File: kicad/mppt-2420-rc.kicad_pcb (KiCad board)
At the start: 4 copper layers, 67.7 x 86.4 mm, 121 parts, among them J1 MKDS 5/ 2-9,5, J2 MKDS 5/ 2-9,5, J3 8P8C, J4 8P8C, J5 Phoenix Contact MC 1,5, J7 UEXT, Q1 IPA045N10N3G, Q2 IPA045N10N3G, Q8 IRF135B203, Q9 DMP10H4D2S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

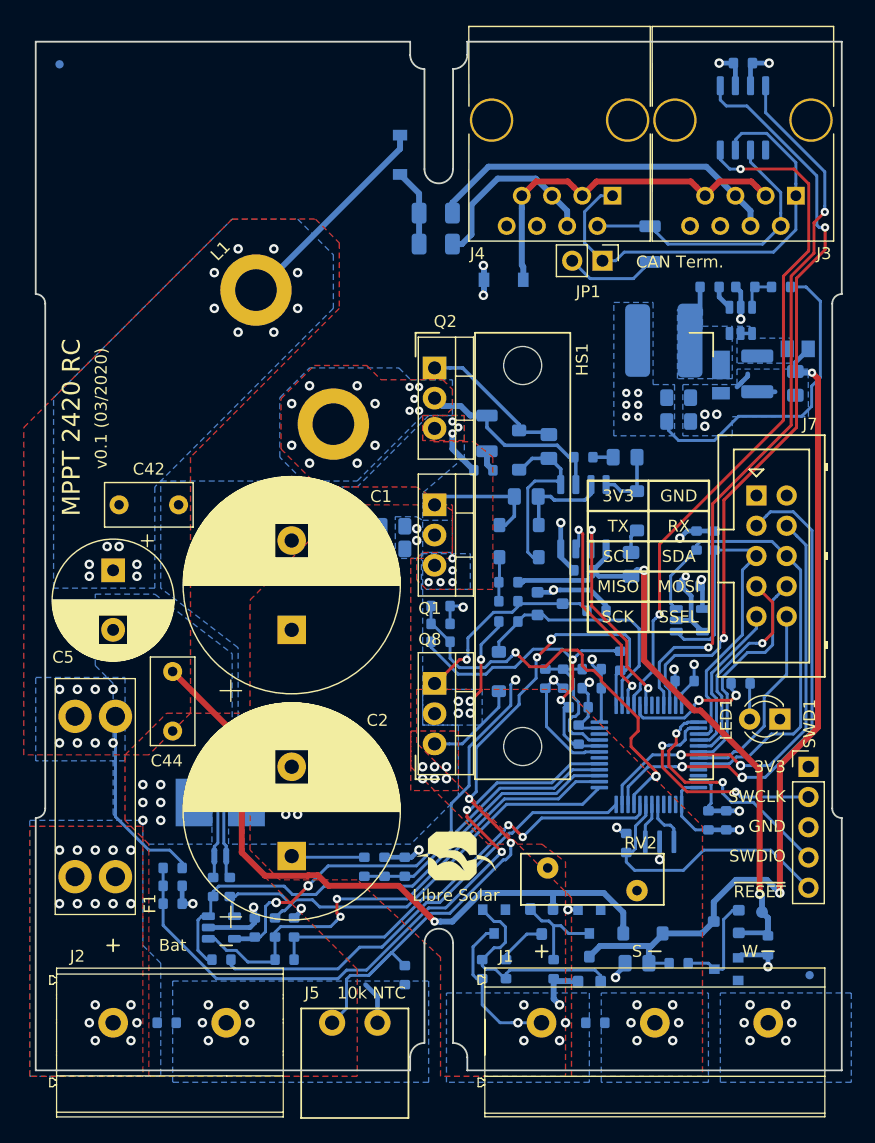
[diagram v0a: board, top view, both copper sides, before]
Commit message: Fix errors after first prototype build-up
- Collision of capacitors with MOSFET clamps
- BOOT0 pin tied to GND
- Assignment of a few previously unasigned passives
- Add optional debug serial connector
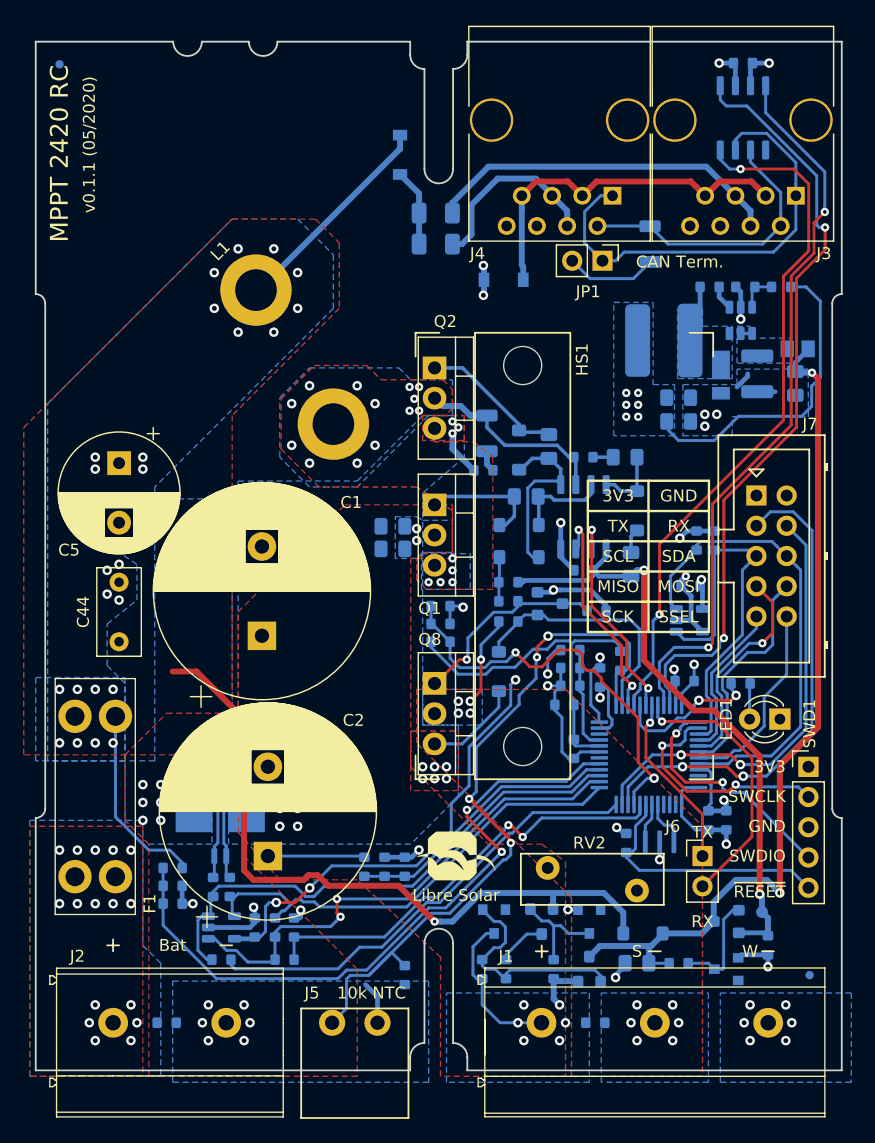
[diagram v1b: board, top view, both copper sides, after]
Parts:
- removed C42: 0.22µF, Capacitor_THT:C_Rect_L7.2mm_W3.5mm_P5.00mm_FKS2_FKP2_MKS2_MKP2
- removed the LOGO1 at (122.5, 61.0)
- added J6: Conn_01x02, Connector_PinHeader_2.54mm:PinHeader_1x02_P2.54mm_Vertical, F.Cu at (156.0, 122.0)
- C15: value 100nF -> 1nF
- C41: value 4.7µF -> 2.2µF
- J1: value MKDS 5/ 2-9,5 -> MKDS 5/ 3-9,5
- Q1, Q2: value IPA045N10N3G -> IPP045N10N3G
- Q8: value IRF135B203 -> IPP045N10N3G
- R15: value ? -> 1k
- R42: value 470R -> 1k
- R60: value 12k -> 33k
- R64, R65, R66: value 12k -> 10k
- RV2: value 56V -> 82V
- moved C5 9.01 mm to (107.0, 89.0)
- moved C44 8.75 mm to (107.0, 104.0)
- moved C1 2.55 mm to (119.0, 103.5)
- moved R40 2.41 mm to (144.9, 104.7), turned to 180 degrees
- moved C39 2.28 mm to (144.9, 106.2), turned to 180 degrees
- moved C2 2.00 mm to (119.5, 122.0)
- moved C48 1.26 mm to (145.2, 113.0), turned to 270 degrees
- moved C49 1.22 mm to (144.4, 109.3), turned to 180 degrees
- moved C32 1.14 mm to (147.4, 107.0), turned to 270 degrees
- moved C34 0.85 mm to (144.9, 107.7), turned to 180 degrees
- moved R6 0.50 mm to (115.5, 118.0)
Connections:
- U2 pad 45: Net-(U2-Pad45) -> GND
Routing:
- net /MCU/USART1_RX: track 0.00 -> 22.8 mm, vias 0 -> 1
- net /MCU/USART1_TX: track 0.00 -> 14.8 mm, vias 0 -> 1
- net VDDA: track 12.1 -> 8.70 mm
- net GND: track 76.3 -> 79.6 mm
- net +3V3: track 92.4 -> 95.7 mm, vias 15 -> 16
- net VBUS: track 91.1 -> 93.3 mm, vias 23 -> 25
- net /MCU/~RESET: track 23.4 -> 21.3 mm
- net /DCDC_HV+: track 24.0 -> 26.0 mm
- net /MCU/LED_PWR: track 11.1 -> 12.5 mm
- net +12V: track 51.8 -> 52.5 mm
- net GNDPWR: track 29.1 -> 28.5 mm, vias 22 -> 23
- net VREF: track 29.7 -> 30.0 mm, vias 2 -> 0
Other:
- outline, holes or cut-outs redrawn
- board text added: "v0.1.1"
- board text added: "v0.1.1 (05/2020)"
- board text removed: "v0.1"
- board text removed: "v0.1 (03/2020)"

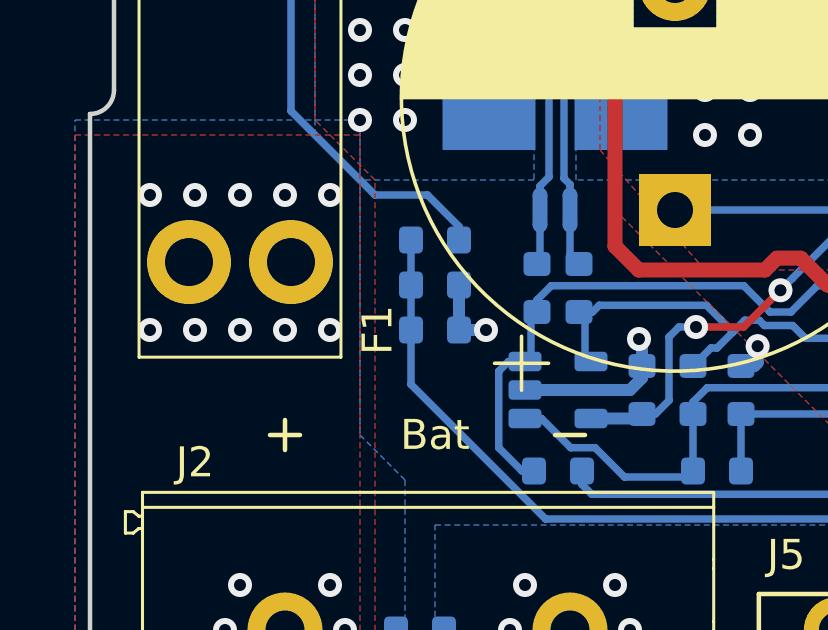
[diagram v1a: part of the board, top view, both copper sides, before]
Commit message: Fix some references and part numbers
See issues #3, #5, #7, #8 and #9.
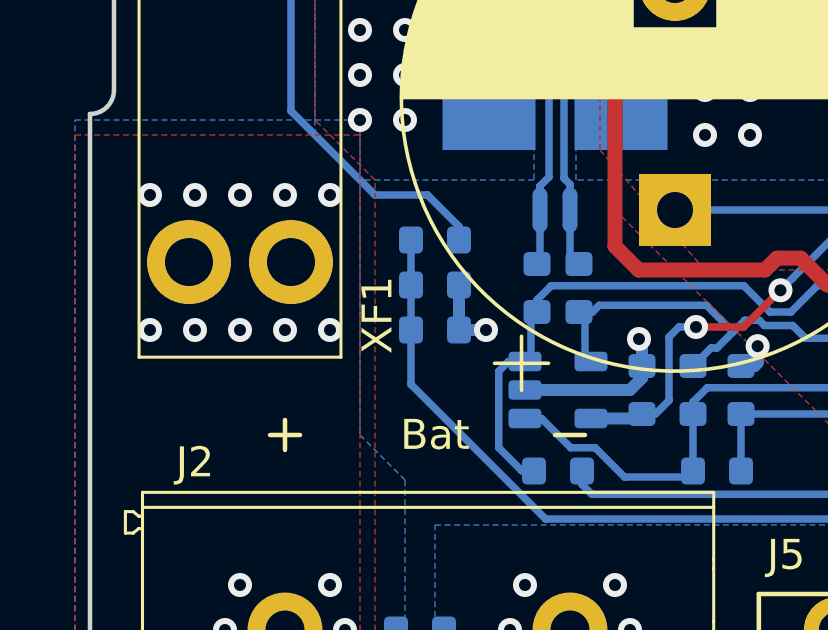
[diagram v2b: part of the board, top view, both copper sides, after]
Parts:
- added XF1: ATO blade fuse, LibreSolar:Keystone-Fuse-3557-2, F.Cu at (105.0, 117.0)
- F1: footprint LibreSolar:Keystone-Fuse-3557-2 -> LibreSolar:NULL
- moved F1 20.4 mm to (117.2, 100.8), turned to 0 degrees
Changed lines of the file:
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@@
     (tracks 1124)
     (zones 0)
-    (modules 120)
+    (modules 121)
     (nets 83)
   )
@@
     (add_net VBUS)
   )
+  (module LibreSolar:NULL (layer Top)
+    (at 117.25 100.75)
+    (fp_text reference F1 (at 0 1) (layer F.SilkS) hide
+      (effects (font (size 1 1) (thickness 0.15)))
+    )
+    (fp_text value 25A (at 0 -1) (layer F.Fab) hide
+      (effects (font (size 1 1) (thickness 0.15)))
+    )
+  )
+  (module LibreSolar:Keystone-Fuse-3557-2 (layer Top)
+    (at 105 117 270)
+    (tags "KEYSTONE, FUSE, ATO, ATC, HOLDER 3557-2")
+    (fp_text reference XF1 (at 8.5 -4 270) (layer F.SilkS)
+      (effects (font (size 1 1) (thickness 0.15)) (justify top))
+    )
+    (fp_text value "ATO blade fuse" (at 0 4.2 90) (layer F.Fab)
+      (effects (font (size 1 1) (thickness 0.15)) (justify top))
+    )
+    (fp_line (start -10 3.5) (end -10 -3.5) (layer F.CrtYd) (width 0.1))
+    (fp_line (start 10 3.5) (end -10 3.5) (layer F.CrtYd) (width 0.1))
+    (fp_line (start 10 -3.5) (end 10 3.5) (layer F.CrtYd) (width 0.1))
+    (fp_line (start -10 -3.5) (end 10 -3.5) (layer F.CrtYd) (width 0.1))
+    (fp_text user %R (at 0 0 90) (layer F.Fab)
+      (effects (font (size 1 1) (thickness 0.15)))
+    )
+    (fp_line (start -9.8 3.4) (end -9.8 -3.4) (layer F.Fab) (width 0.1))
+    (fp_line (start 9.8 3.4) (end -9.8 3.4) (layer F.Fab) (width 0.1))
+    (fp_line (start 9.8 -3.4) (end 9.8 3.4) (layer F.Fab) (width 0.1))
+    (fp_line (start -9.8 -3.4) (end 9.8 -3.4) (layer F.Fab) (width 0.1))
+    (fp_line (start -9.905 3.365) (end -9.905 -3.365) (layer F.SilkS) (width 0.1))
+    (fp_line (start 9.905 3.365) (end -9.905 3.365) (layer F.SilkS) (width 0.1))
+    (fp_line (start 9.905 -3.365) (end 9.905 3.365) (layer F.SilkS) (width 0.1))
+    (fp_line (start -9.905 -3.365) (end 9.905 -3.365) (layer F.SilkS) (width 0.1))
+    (pad 2 thru_hole circle (at 6.735 1.7) (size 2.8 2.8) (drill 1.6) (layers *.Cu *.Mask)
+      (net 31 /BAT+))
+    (pad 2 thru_hole circle (at 6.735 -1.7) (size 2.8 2.8) (drill 1.6) (layers *.Cu *.Mask)
+      (net 31 /BAT+))
+    (pad 1 thru_hole circle (at -6.735 1.7) (size 2.8 2.8) (drill 1.6) (layers *.Cu *.Mask)
+      (net 40 VBUS))
+    (pad 1 thru_hole circle (at -6.735 -1.7) (size 2.8 2.8) (drill 1.6) (layers *.Cu *.Mask)
+      (net 40 VBUS))
+    (model ${KISYS3DMOD}/LibreSolar.3dshapes/Keystone-3557-2_fuse.stp
+      (offset (xyz 0 -0.2999999954944519 3.299999950438973))
+      (scale (xyz 1 1 1))
+      (rotate (xyz -90 0 0))
+    )
+  )
   (module Connector_PinHeader_2.54mm:PinHeader_1x02_P2.54mm_Vertical (layer Top)
     (at 156 122)
@@
     )
   )
-  (module LibreSolar:Keystone-Fuse-3557-2 (layer Top)
-    (at 105 117 270)
-    (tags "KEYSTONE, FUSE, ATO, ATC, HOLDER 3557-2")
-    (fp_text reference F1 (at 9 -4 270) (layer F.SilkS)
-      (effects (font (size 1 1) (thickness 0.15)) (justify top))
-    )
-    (fp_text value 25A (at 0 4.2 90) (layer F.Fab)
-      (effects (font (size 1 1) (thickness 0.15)) (justify top))
-    )
-    (fp_line (start -9.905 -3.365) (end 9.905 -3.365) (layer F.SilkS) (width 0.1))
-    (fp_line (start 9.905 -3.365) (end 9.905 3.365) (layer F.SilkS) (width 0.1))
-    (fp_line (start 9.905 3.365) (end -9.905 3.365) (layer F.SilkS) (width 0.1))
-    (fp_line (start -9.905 3.365) (end -9.905 -3.365) (layer F.SilkS) (width 0.1))
-    (fp_line (start -9.8 -3.4) (end 9.8 -3.4) (layer F.Fab) (width 0.1))
-    (fp_line (start 9.8 -3.4) (end 9.8 3.4) (layer F.Fab) (width 0.1))
-    (fp_line (start 9.8 3.4) (end -9.8 3.4) (layer F.Fab) (width 0.1))
-    (fp_line (start -9.8 3.4) (end -9.8 -3.4) (layer F.Fab) (width 0.1))
-    (fp_text user %R (at 0 0 90) (layer F.Fab)
-      (effects (font (size 1 1) (thickness 0.15)))
-    )
-    (fp_line (start -10 -3.5) (end 10 -3.5) (layer F.CrtYd) (width 0.1))
-    (fp_line (start 10 -3.5) (end 10 3.5) (layer F.CrtYd) (width 0.1))
-    (fp_line (start 10 3.5) (end -10 3.5) (layer F.CrtYd) (width 0.1))
-    (fp_line (start -10 3.5) (end -10 -3.5) (layer F.CrtYd) (width 0.1))
-    (pad 1 thru_hole circle (at -6.735 -1.7) (size 2.8 2.8) (drill 1.6) (layers *.Cu *.Mask)
-      (net 40 VBUS))
-    (pad 1 thru_hole circle (at -6.735 1.7) (size 2.8 2.8) (drill 1.6) (layers *.Cu *.Mask)
-      (net 40 VBUS))
-    (pad 2 thru_hole circle (at 6.735 -1.7) (size 2.8 2.8) (drill 1.6) (layers *.Cu *.Mask)
-      (net 31 /BAT+))
-    (pad 2 thru_hole circle (at 6.735 1.7) (size 2.8 2.8) (drill 1.6) (layers *.Cu *.Mask)
-      (net 31 /BAT+))
-    (model ${KISYS3DMOD}/LibreSolar.3dshapes/Keystone-3557-2_fuse.stp
-      (offset (xyz 0 -0.2999999954944519 3.299999950438973))
-      (scale (xyz 1 1 1))
-      (rotate (xyz -90 0 0))
-    )
-  )

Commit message: Clean up BOM and add build folder for generated files
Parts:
- D2, D3: value D_Schottky -> NRVTS260ESFT1G
- U6: value 24AA01 -> 24AA32
- moved F1 52.0 mm to (106.0, 151.5)
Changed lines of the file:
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@@
   )
   (module LibreSolar:NULL (layer Top)
-    (at 117.25 100.75)
+    (at 106 151.5)
+    (attr virtual)
     (fp_text reference F1 (at 0 1) (layer F.SilkS) hide
       (effects (font (size 1 1) (thickness 0.15)))
@@
       (effects (font (size 1 1) (thickness 0.15)) (justify mirror))
     )
-    (fp_text value D_Schottky (at 0 -2.1) (layer B.Fab)
+    (fp_text value NRVTS260ESFT1G (at 0 -2.1) (layer B.Fab)
       (effects (font (size 1 1) (thickness 0.15)) (justify mirror))
     )
@@
       (effects (font (size 1 1) (thickness 0.15)) (justify mirror))
     )
-    (fp_text value D_Schottky (at 0 -2.1 90) (layer B.Fab)
+    (fp_text value NRVTS260ESFT1G (at 0 -2.1 90) (layer B.Fab)
       (effects (font (size 1 1) (thickness 0.15)) (justify mirror))
     )
@@
       (effects (font (size 1 1) (thickness 0.15)) (justify mirror))
     )
-    (fp_text value 24AA01 (at 0 -2.9) (layer B.Fab)
-      (effects (font (size 1 1) (thickness 0.15)) (justify mirror))
-    )
+    (fp_text value 24AA32 (at 0 -2.9) (layer B.Fab)
+      (effects (font (size 1 1) (thickness 0.15)) (justify mirror))
+    )
